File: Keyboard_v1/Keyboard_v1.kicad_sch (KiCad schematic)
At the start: 14 parts, among them SW1 SW_Push, U1 ATmega32U4-A, Y1 16MHz

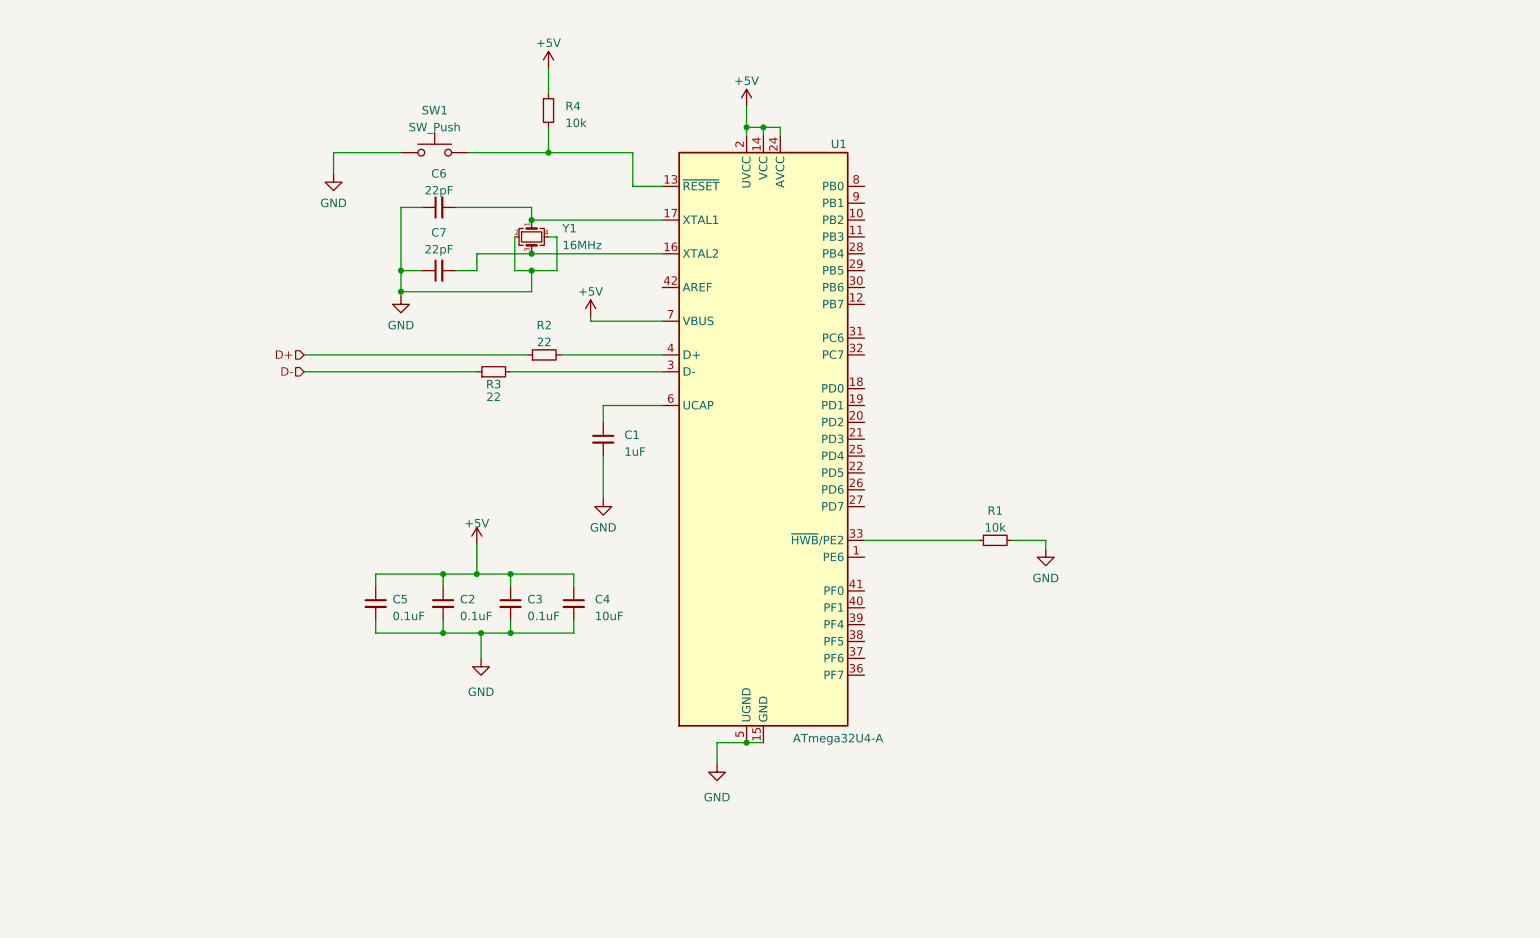
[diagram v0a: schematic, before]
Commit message: added switch matrix and component footprints
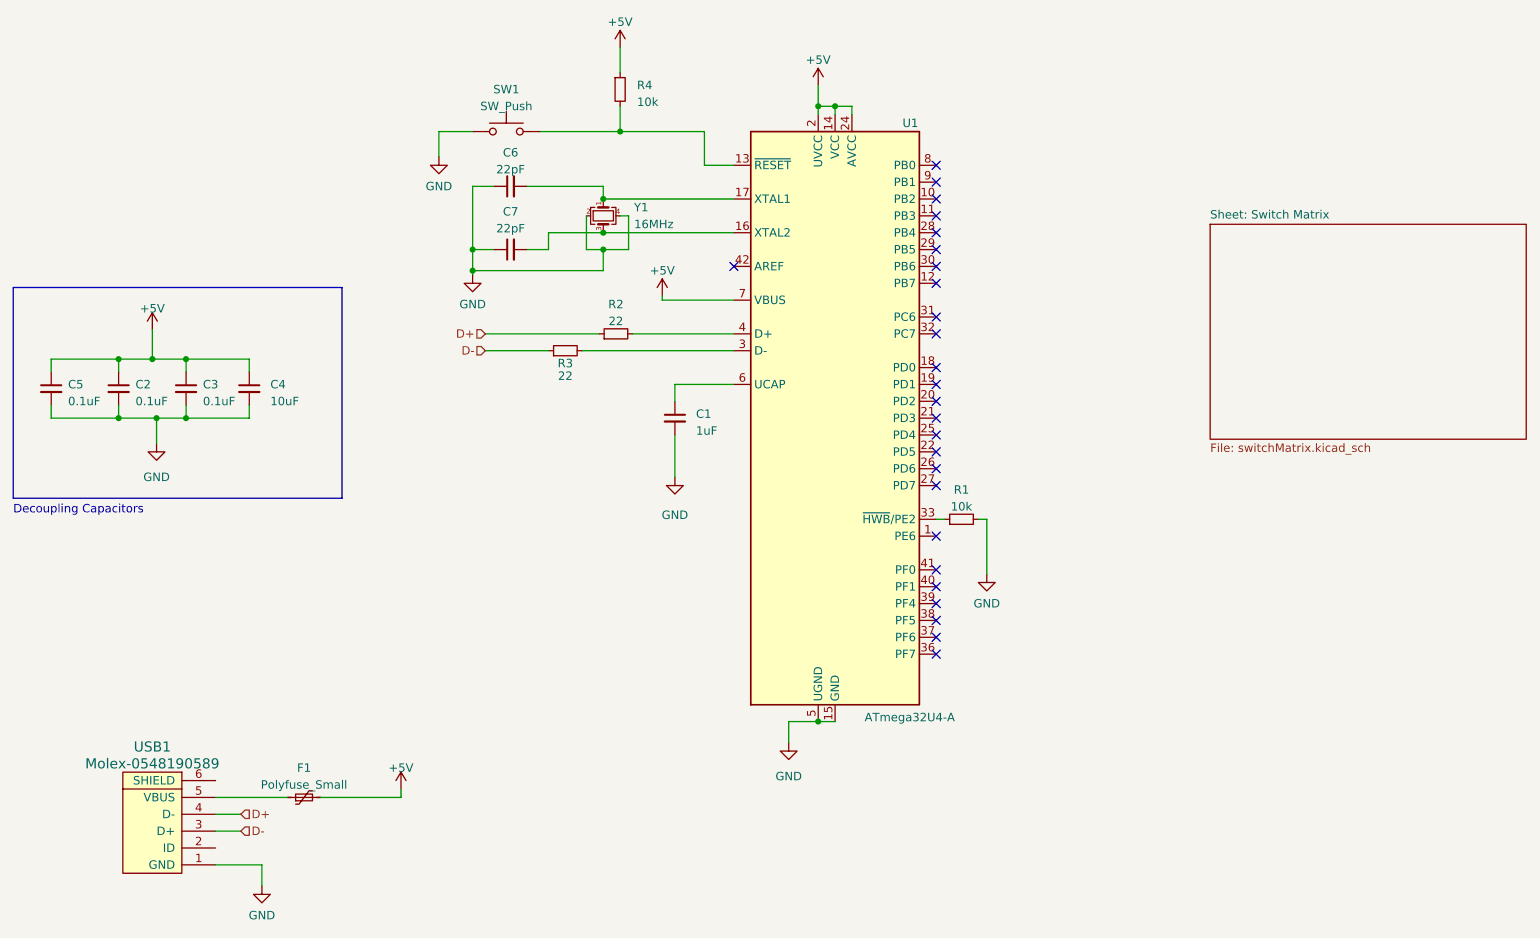
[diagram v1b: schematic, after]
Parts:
- added F1: Polyfuse_Small, Fuse:Fuse_1206_3216Metric, symbol Device:Polyfuse_Small
- added USB1: Molex-0548190589, random-keyboard-parts:Molex-0548190589, symbol random-keyboard-parts:Molex-0548190589
- C1, C2, C3, C4, C5, C6, C7: footprint (none) -> Capacitor_SMD:C_0805_2012Metric
- R1, R2, R3, R4: footprint (none) -> Resistor_SMD:R_0805_2012Metric
- SW1: footprint (none) -> random-keyboard-parts:SKQG-1155865
- Y1: footprint (none) -> Crystal:Crystal_SMD_3225-4Pin_3.2x2.5mm
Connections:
- net +5V: now also F1.2
- net D+: now also USB1.4 (D-)
- net D-: now also USB1.3 (D+)
- net GND: now also USB1.1 (GND)
- new net: F1.1, USB1.5 (VBUS)
- no-connect marks 0 -> 26
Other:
- added sheet Sheet: Switch Matrix (switchMatrix.kicad_sch)
- note added: "Decoupling Capacitors"
- moved on the sheet: C1, C2, C3, C4, C5, C6, C7, R1, R2, R3, R4, SW1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
